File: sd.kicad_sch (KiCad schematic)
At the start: 9 parts, among them J602 Micro_SD_Card

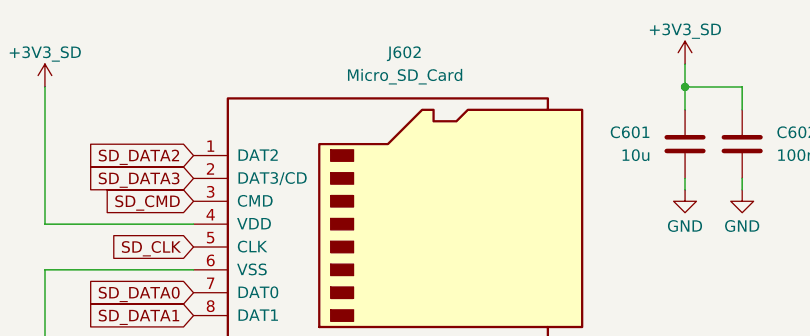
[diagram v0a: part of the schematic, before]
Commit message: feat: restart routing ddr
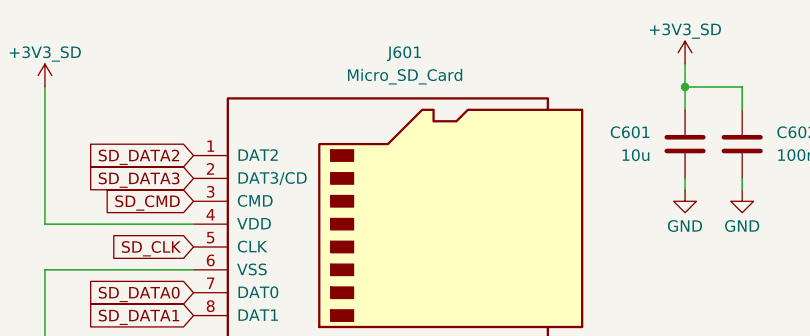
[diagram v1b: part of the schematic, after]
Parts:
- C602: footprint (none) -> Capacitor_SMD:C_0402_1005Metric
- renumbered J602 to J601
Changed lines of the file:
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@@
 		(in_pos_files yes)
 		(dnp no)
-		(property "Reference" "#PWR0607"
+		(property "Reference" "#PWR0608"
 			(at 209.55 83.82 0)
 			(hide yes)
@@
 			(project "ZYNQ_Pi_Zero"
 				(path "/239d02af-7f9c-469f-b86b-abe2695ec54e/3cf6dfc2-a0f8-40c2-9f99-77c1321743b1"
-					(reference "#PWR0607")
+					(reference "#PWR0608")
 					(unit 1)
 				)
@@
 		(in_pos_files yes)
 		(dnp no)
-		(property "Reference" "#PWR0605"
+		(property "Reference" "#PWR0606"
 			(at 201.93 110.49 0)
 			(hide yes)
@@
 			(project "ZYNQ_Pi_Zero"
 				(path "/239d02af-7f9c-469f-b86b-abe2695ec54e/3cf6dfc2-a0f8-40c2-9f99-77c1321743b1"
-					(reference "#PWR0605")
+					(reference "#PWR0606")
 					(unit 1)
 				)
@@
 		(dnp no)
 		(fields_autoplaced yes)
-		(property "Reference" "J602"
+		(property "Reference" "J601"
 			(at 178.435 62.23 0)
 			(show_name no)
@@
 			(project "ZYNQ_Pi_Zero"
 				(path "/239d02af-7f9c-469f-b86b-abe2695ec54e/3cf6dfc2-a0f8-40c2-9f99-77c1321743b1"
-					(reference "J602")
+					(reference "J601")
 					(unit 1)
 				)
@@
 		(in_pos_files yes)
 		(dnp no)
-		(property "Reference" "#PWR0608"
+		(property "Reference" "#PWR0609"
 			(at 215.9 83.82 0)
 			(hide yes)
@@
 			(project "ZYNQ_Pi_Zero"
 				(path "/239d02af-7f9c-469f-b86b-abe2695ec54e/3cf6dfc2-a0f8-40c2-9f99-77c1321743b1"
-					(reference "#PWR0608")
+					(reference "#PWR0609")
 					(unit 1)
 				)
@@
 		(in_pos_files yes)
 		(dnp no)
-		(property "Reference" "#PWR0603"
+		(property "Reference" "#PWR0604"
 			(at 138.43 69.85 0)
 			(hide yes)
@@
 			(project "ZYNQ_Pi_Zero"
 				(path "/239d02af-7f9c-469f-b86b-abe2695ec54e/3cf6dfc2-a0f8-40c2-9f99-77c1321743b1"
-					(reference "#PWR0603")
+					(reference "#PWR0604")
 					(unit 1)
 				)
@@
 		(in_pos_files yes)
 		(dnp no)
-		(property "Reference" "#PWR0604"
+		(property "Reference" "#PWR0605"
 			(at 138.43 110.49 0)
 			(hide yes)
@@
 			(project "ZYNQ_Pi_Zero"
 				(path "/239d02af-7f9c-469f-b86b-abe2695ec54e/3cf6dfc2-a0f8-40c2-9f99-77c1321743b1"
-					(reference "#PWR0604")
+					(reference "#PWR0605")
 					(unit 1)
 				)
@@
 		(in_pos_files yes)
 		(dnp no)
-		(property "Reference" "#PWR0602"
+		(property "Reference" "#PWR0603"
 			(at 124.46 69.85 0)
 			(hide yes)
@@
 			(project "ZYNQ_Pi_Zero"
 				(path "/239d02af-7f9c-469f-b86b-abe2695ec54e/3cf6dfc2-a0f8-40c2-9f99-77c1321743b1"
-					(reference "#PWR0602")
+					(reference "#PWR0603")
 					(unit 1)
 				)
@@
 			)
 		)
-		(property "Footprint" ""
+		(property "Footprint" "Capacitor_SMD:C_0402_1005Metric"
 			(at 216.8652 76.2 0)
 			(hide yes)
@@
 		(in_pos_files yes)
 		(dnp no)
-		(property "Reference" "#PWR0606"
+		(property "Reference" "#PWR0602"
 			(at 110.49 87.63 0)
 			(hide yes)
@@
 			(project "ZYNQ_Pi_Zero"
 				(path "/239d02af-7f9c-469f-b86b-abe2695ec54e/3cf6dfc2-a0f8-40c2-9f99-77c1321743b1"
-					(reference "#PWR0606")
+					(reference "#PWR0602")
 					(unit 1)
 				)
@@
 		(in_pos_files yes)
 		(dnp no)
-		(property "Reference" "#PWR0609"
+		(property "Reference" "#PWR0607"
 			(at 209.55 67.31 0)
 			(hide yes)
@@
 			(project "ZYNQ_Pi_Zero"
 				(path "/239d02af-7f9c-469f-b86b-abe2695ec54e/3cf6dfc2-a0f8-40c2-9f99-77c1321743b1"
-					(reference "#PWR0609")
-					(unit 1)
-				)
+					(reference "#PWR0607")
+					(unit 1)
+				)
